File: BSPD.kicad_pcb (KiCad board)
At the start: 2 copper layers, 160 x 145 mm, 66 parts, among them J1 Microfit_01x02_Vertical, J2 Conn_01x39_Male, Q1 DMN6075SQ-7, U1 LM7805, U2 LM7902D, U3 CD4081BM96, U4 CD4071BM96, U5 LM7902D, U6 LM7902D, U7 P783-Q24-S12-S, U8 Raspberry_Pi_4

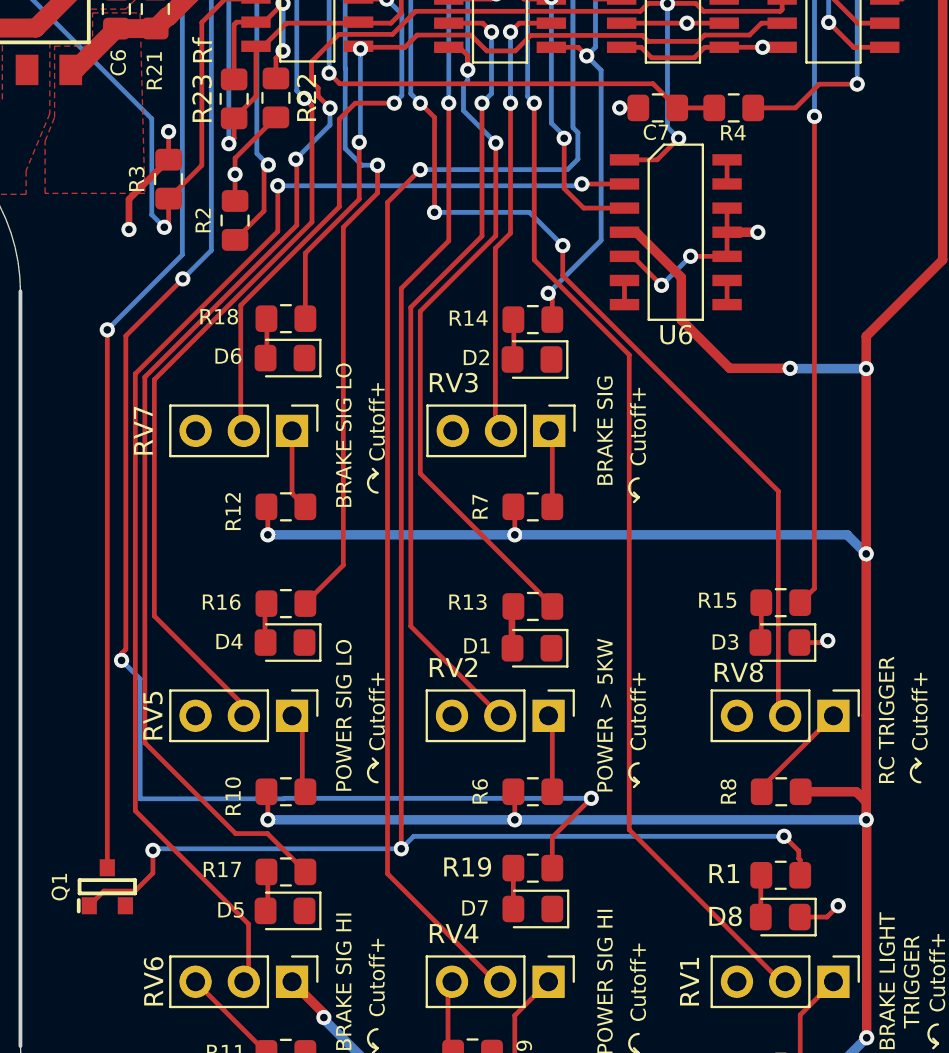
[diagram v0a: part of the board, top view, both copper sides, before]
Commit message: Switched D7 and R19 with D3 and R15
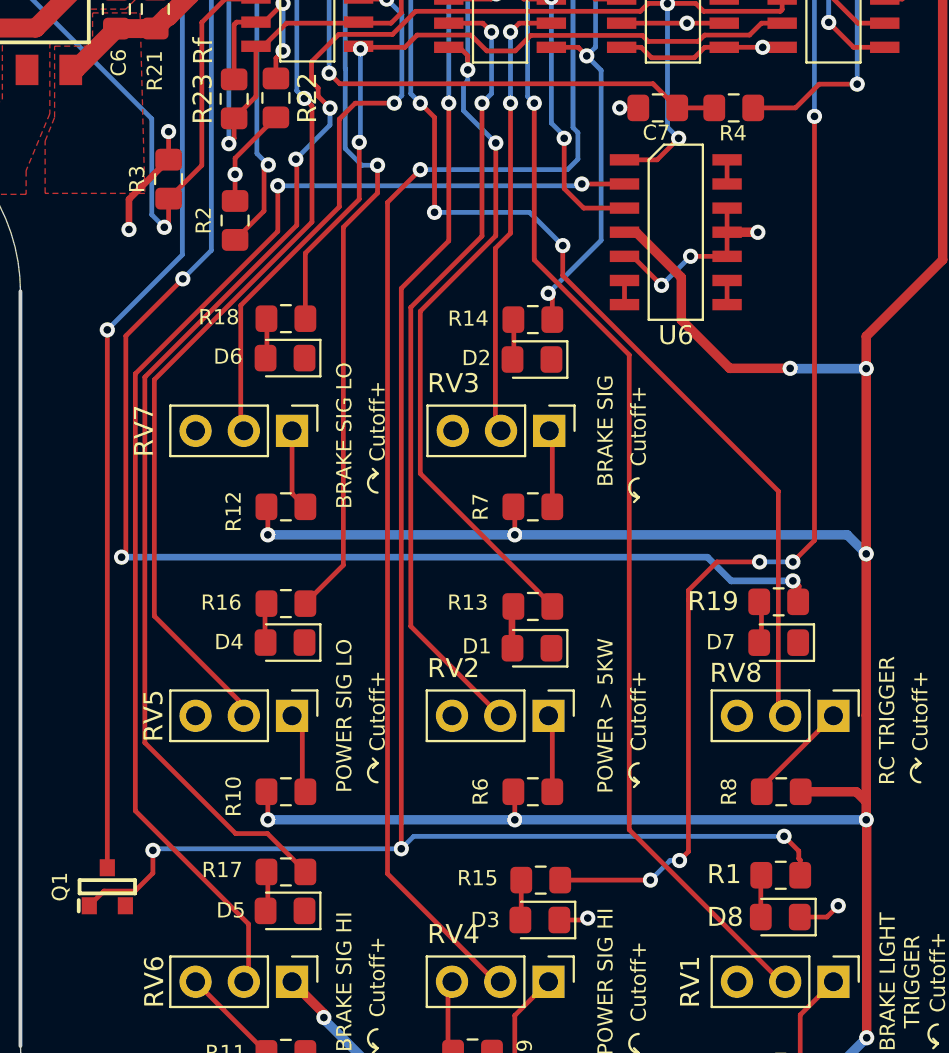
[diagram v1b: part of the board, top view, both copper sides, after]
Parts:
- moved R15 19.3 mm to (141.5, 150.2)
- moved D3 19.3 mm to (141.4, 152.3)
- moved D7 19.1 mm to (154.0, 137.8)
- moved R19 19.1 mm to (154.0, 135.6)
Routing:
- net Net-(R15-Pad1): track 53.5 -> 78.7 mm, vias 2 -> 6
- net BSPD_TRIGGER: track 174.9 -> 170.5 mm
